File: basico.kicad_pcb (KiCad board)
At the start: 2 copper layers, 85.7 x 60.3 mm, 14 parts, among them P1 Power, P10 CONN_01X01, P11 CONN_01X01, P12 CONN_01X01, P13 CONN_01X01, P2 Analog, P3 Analog, P4 Digital, P5 PWM, P6 PWM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

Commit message: Update PCB
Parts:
- moved P4 91.6 mm to (82.0, 126.5)
- moved P3 59.1 mm to (81.0, 101.0), turned to 270 degrees
- moved P7 56.4 mm to (126.0, 103.0), turned to 270 degrees
- moved P6 50.9 mm to (124.5, 78.5), turned to 270 degrees
- moved P5 44.3 mm to (125.0, 50.5), turned to 270 degrees
- moved P2 31.0 mm to (81.0, 77.5), turned to 270 degrees
- moved P1 29.3 mm to (81.0, 50.5), turned to 270 degrees
- moved P10 21.4 mm to (101.1, 36.2)
- moved P11 21.4 mm to (106.8, 36.2)
- moved P12 21.4 mm to (112.5, 36.2)
- moved P13 21.4 mm to (118.2, 36.2)
- moved P8 21.4 mm to (89.6, 36.2)
- moved P9 21.4 mm to (95.4, 36.2)
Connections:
- P2 pad 1: (no net) -> /Ar_A0
- P2 pad 2: (no net) -> /Ar_A1
- P2 pad 3: (no net) -> /Ar_A2
- P2 pad 4: (no net) -> /Ar_A3
- P2 pad 5: (no net) -> /Ar_A4
- P2 pad 6: (no net) -> /Ar_A5
- P2 pad 7: (no net) -> /Ar_A6
- P2 pad 8: (no net) -> /Ar_A7
- P3 pad 1: (no net) -> /Ar_A8
- P3 pad 6: (no net) -> /Ar_A13
- P4 pad 11: (no net) -> /Ar_44
- P4 pad 13: (no net) -> /Ar_42
- P4 pad 15: (no net) -> /Ar_40
- P4 pad 17: (no net) -> /Ar_38
- P4 pad 19: (no net) -> /Ar_36
- P4 pad 21: (no net) -> /Ar_34
- P4 pad 25: (no net) -> /Ar_30
- P4 pad 27: (no net) -> /Ar_28
- P4 pad 29: (no net) -> /Ar_26
- P4 pad 3: (no net) -> /Ar_52
- P4 pad 31: (no net) -> /Ar_24
- P4 pad 4: (no net) -> /Ar_53
- P4 pad 5: (no net) -> /Ar_50
- P4 pad 6: (no net) -> /Ar_51
- P4 pad 7: (no net) -> /Ar_48
- P4 pad 8: (no net) -> /Ar_49
- P4 pad 9: (no net) -> /Ar_46
- P5 pad 10: (no net) -> /Ar_8
- P5 pad 7: (no net) -> /Ar_11
- P5 pad 8: (no net) -> /Ar_10
- P5 pad 9: (no net) -> /Ar_9
- P6 pad 4: (no net) -> /Ar_4
- P6 pad 5: (no net) -> /Ar_3
- P7 pad 1: (no net) -> /Ar_14
- P7 pad 3: (no net) -> /Ar_16
- P7 pad 4: (no net) -> /Ar_17
- P7 pad 5: (no net) -> /Ar_18
- P7 pad 7: (no net) -> /Ar_20
- P7 pad 8: (no net) -> /Ar_21
- XA101 pad 11: (no net) -> /Ar_10
- XA101 pad 13: (no net) -> /Ar_9
- XA101 pad 19: (no net) -> /Ar_20
- XA101 pad 21: (no net) -> /Ar_21
- XA101 pad 23: (no net) -> /Ar_8
- XA101 pad 25: (no net) -> /Ar_9
- XA101 pad 27: (no net) -> /Ar_10
- XA101 pad 29: (no net) -> /Ar_30
- XA101 pad 31: (no net) -> /Ar_3
- XA101 pad 33: (no net) -> /Ar_18
- XA101 pad 34: (no net) -> /Ar_34
- XA101 pad 35: (no net) -> /Ar_24
- XA101 pad 36: (no net) -> /Ar_26
- XA101 pad 37: (no net) -> /Ar_28
- XA101 pad 39: (no net) -> /Ar_14
- XA101 pad 44: (no net) -> /Ar_A0
- XA101 pad 46: (no net) -> /Ar_A1
- XA101 pad 48: (no net) -> /Ar_A2
- XA101 pad 49: (no net) -> /Ar_A6
- XA101 pad 50: (no net) -> /Ar_A7
- XA101 pad 52: (no net) -> /Ar_A8
- XA101 pad 54: (no net) -> /Ar_11
- XA101 pad 56: (no net) -> /Ar_4
- XA101 pad 58: (no net) -> /Ar_50
- XA101 pad 60: (no net) -> /Ar_52
- XA101 pad 61: (no net) -> /Ar_51
- XA101 pad 62: (no net) -> /Ar_A13
- XA101 pad 63: (no net) -> /Ar_17
- XA101 pad 64: (no net) -> /Ar_16
- XA101 pad 66: (no net) -> /Ar_A3
- XA101 pad 68: (no net) -> /Ar_44
- XA101 pad 69: (no net) -> /Ar_38
- XA101 pad 70: (no net) -> /Ar_A5
- XA101 pad 71: (no net) -> /Ar_48
- XA101 pad 72: (no net) -> /Ar_46
- XA101 pad 73: (no net) -> /Ar_A4
- XA101 pad 74: (no net) -> /Ar_36
- XA101 pad 75: (no net) -> /Ar_42
- XA101 pad 76: (no net) -> /Ar_40
- XA101 pad 78: (no net) -> /Ar_49
- XA101 pad 80: (no net) -> /Ar_53
- XA101 pad 9: (no net) -> /Ar_11

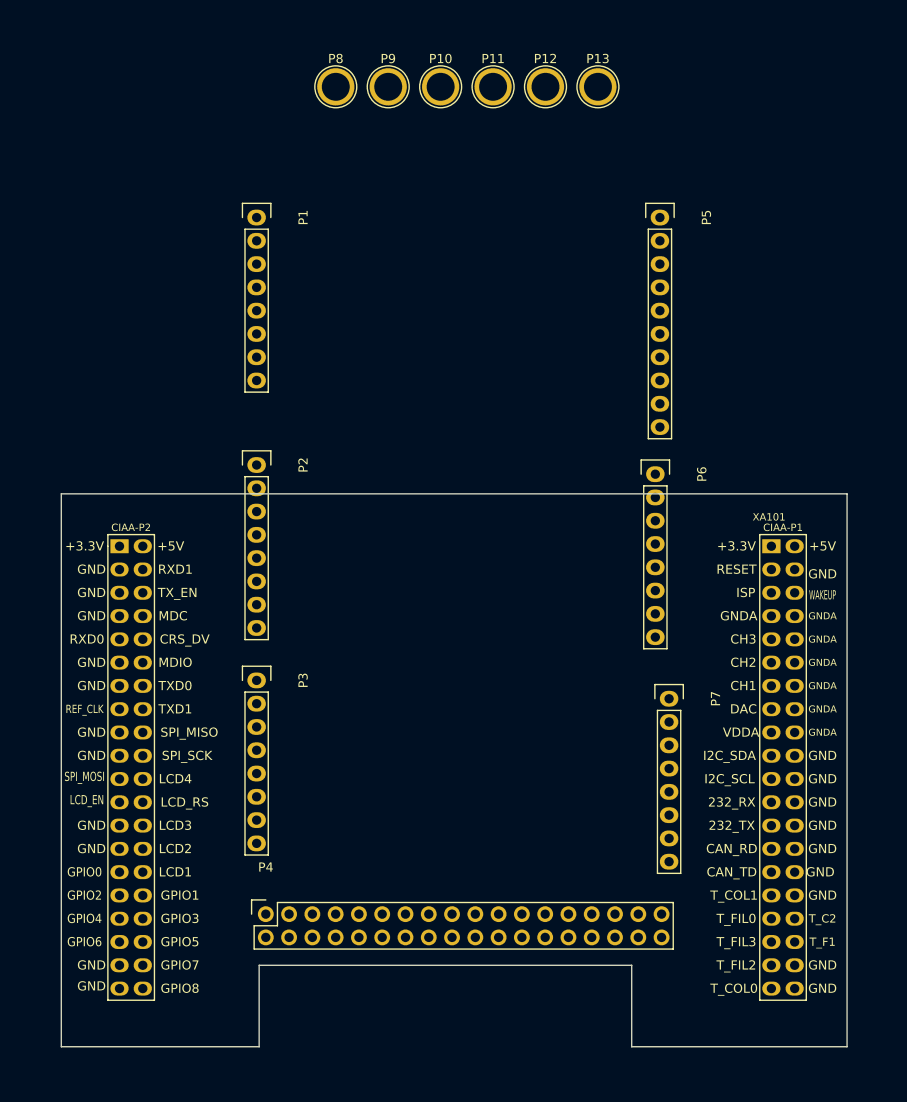
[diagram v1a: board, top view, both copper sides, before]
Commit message: Remove unused components. Update PCB
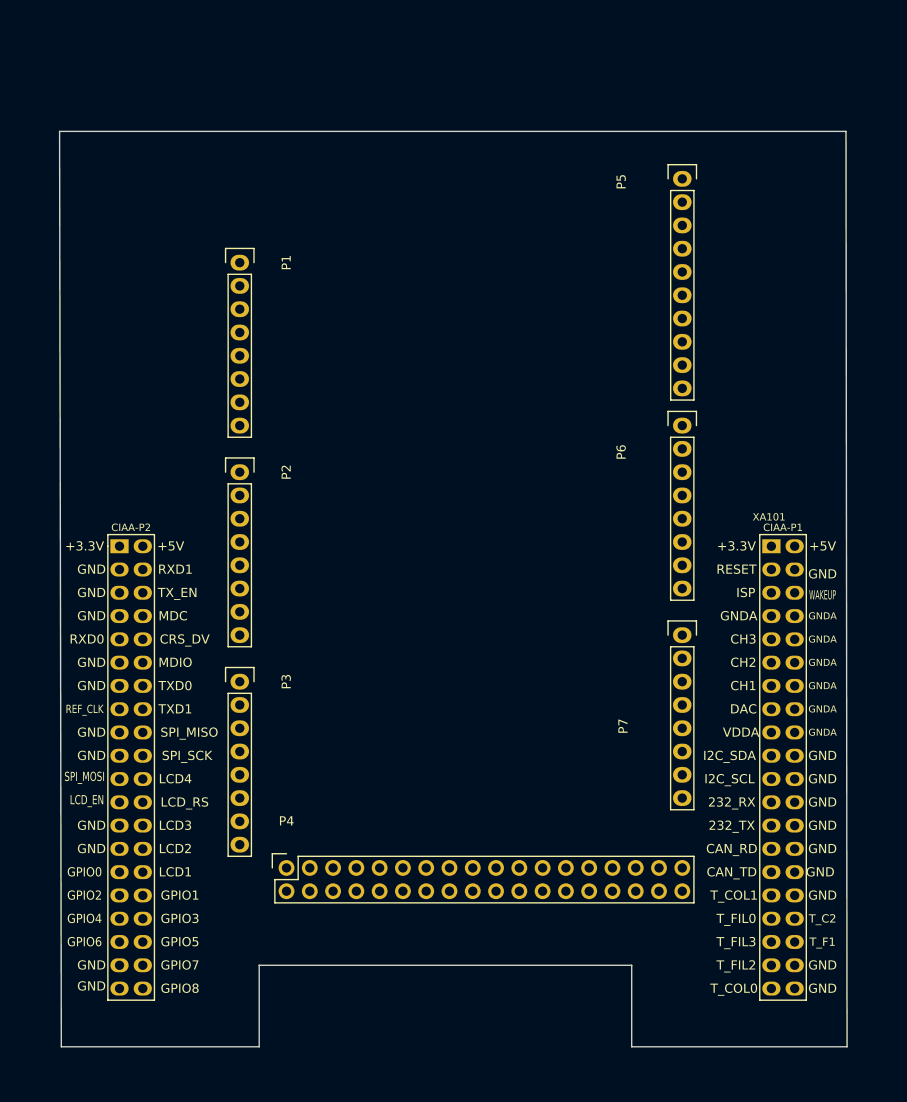
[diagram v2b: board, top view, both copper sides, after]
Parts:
- removed P10, P11, P12, P13, P8, P9: CONN_01X01, footprint:Arduino_1pin
- moved P7 7.09 mm to (127.4, 96.1)
- moved P6 6.06 mm to (127.4, 73.2)
- moved P4 5.52 mm to (84.3, 121.5)
- moved P1 5.25 mm to (79.2, 55.4)
- moved P5 4.87 mm to (127.4, 46.3)
- moved P2 2.00 mm to (79.2, 78.3)
- moved P3 1.85 mm to (79.2, 101.1)
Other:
- board size 85.7 x 60.3 mm -> 85.9 x 99.9 mm
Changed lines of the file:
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@@
     (tracks 0)
     (zones 0)
-    (modules 14)
+    (modules 8)
     (nets 44)
   )
@@
     (add_net +3.3VP)
     (add_net +5V)
-    (add_net /Ar_0)
-    (add_net /Ar_1)
     (add_net /Ar_10)
     (add_net /Ar_11)
-    (add_net /Ar_12)
-    (add_net /Ar_13)
     (add_net /Ar_14)
-    (add_net /Ar_15)
     (add_net /Ar_16)
     (add_net /Ar_17)
     (add_net /Ar_18)
-    (add_net /Ar_19)
-    (add_net /Ar_2)
     (add_net /Ar_20)
     (add_net /Ar_21)
-    (add_net /Ar_22)
-    (add_net /Ar_23)
     (add_net /Ar_24)
-    (add_net /Ar_25)
     (add_net /Ar_26)
-    (add_net /Ar_27)
     (add_net /Ar_28)
-    (add_net /Ar_29)
     (add_net /Ar_3)
     (add_net /Ar_30)
-    (add_net /Ar_31)
-    (add_net /Ar_32)
-    (add_net /Ar_33)
     (add_net /Ar_34)
-    (add_net /Ar_35)
     (add_net /Ar_36)
-    (add_net /Ar_37)
     (add_net /Ar_38)
-    (add_net /Ar_39)
     (add_net /Ar_4)
     (add_net /Ar_40)
-    (add_net /Ar_41)
     (add_net /Ar_42)
-    (add_net /Ar_43)
     (add_net /Ar_44)
-    (add_net /Ar_45)
     (add_net /Ar_46)
-    (add_net /Ar_47)
     (add_net /Ar_48)
     (add_net /Ar_49)
-    (add_net /Ar_5)
     (add_net /Ar_50)
     (add_net /Ar_51)
     (add_net /Ar_52)
     (add_net /Ar_53)
-    (add_net /Ar_6)
-    (add_net /Ar_7)
     (add_net /Ar_8)
     (add_net /Ar_9)
     (add_net /Ar_A0)
     (add_net /Ar_A1)
-    (add_net /Ar_A10)
-    (add_net /Ar_A11)
-    (add_net /Ar_A12)
     (add_net /Ar_A13)
-    (add_net /Ar_A14)
-    (add_net /Ar_A15)
     (add_net /Ar_A2)
     (add_net /Ar_A3)
@@
     (add_net /Ar_A7)
     (add_net /Ar_A8)
-    (add_net /Ar_A9)
-    (add_net /Ar_AREF)
-    (add_net /Ar_IOREF)
-    (add_net /Ar_Reset)
-    (add_net /Ar_SCL)
-    (add_net /Ar_SDA)
-    (add_net /Ar_Vin)
     (add_net GND)
     (add_net GNDA)
-    (add_net "Net-(P1-Pad1)")
-    (add_net "Net-(P10-Pad1)")
-    (add_net "Net-(P11-Pad1)")
-    (add_net "Net-(P12-Pad1)")
-    (add_net "Net-(P13-Pad1)")
-    (add_net "Net-(P8-Pad1)")
-    (add_net "Net-(P9-Pad1)")
-    (add_net "Net-(XA101-Pad15)")
-    (add_net "Net-(XA101-Pad17)")
-    (add_net "Net-(XA101-Pad3)")
-    (add_net "Net-(XA101-Pad5)")
-    (add_net "Net-(XA101-Pad55)")
-    (add_net "Net-(XA101-Pad6)")
-  )
-  (module footprint:Arduino_1pin (layer F.Cu)
-    (at 118.236 36.236)
-    (descr "module 1 pin (ou trou mecanique de percage)")
-    (tags DEV)
-    (fp_text reference P13 (at 0 -3.048) (layer F.SilkS)
-      (effects (font (size 1 1) (thickness 0.15)))
-    )
-    (fp_text value CONN_01X01 (at 0 2.794) (layer F.Fab)
-      (effects (font (size 1 1) (thickness 0.15)))
-    )
-    (fp_circle (center 0 0) (end 0 -2.286) (layer F.SilkS) (width 0.15))
-    (pad 1 thru_hole circle (at 0 0) (size 4.064 4.064) (drill 3.048) (layers *.Cu *.Mask F.SilkS))
-  )
-  (module footprint:Arduino_1pin (layer F.Cu)
-    (at 112.516 36.236)
-    (descr "module 1 pin (ou trou mecanique de percage)")
-    (tags DEV)
-    (fp_text reference P12 (at 0 -3.048) (layer F.SilkS)
-      (effects (font (size 1 1) (thickness 0.15)))
-    )
-    (fp_text value CONN_01X01 (at 0 2.794) (layer F.Fab)
-      (effects (font (size 1 1) (thickness 0.15)))
-    )
-    (fp_circle (center 0 0) (end 0 -2.286) (layer F.SilkS) (width 0.15))
-    (pad 1 thru_hole circle (at 0 0) (size 4.064 4.064) (drill 3.048) (layers *.Cu *.Mask F.SilkS))
-  )
-  (module footprint:Arduino_1pin (layer F.Cu)
-    (at 106.796 36.236)
-    (descr "module 1 pin (ou trou mecanique de percage)")
-    (tags DEV)
-    (fp_text reference P11 (at 0 -3.048) (layer F.SilkS)
-      (effects (font (size 1 1) (thickness 0.15)))
-    )
-    (fp_text value CONN_01X01 (at 0 2.794) (layer F.Fab)
-      (effects (font (size 1 1) (thickness 0.15)))
-    )
-    (fp_circle (center 0 0) (end 0 -2.286) (layer F.SilkS) (width 0.15))
-    (pad 1 thru_hole circle (at 0 0) (size 4.064 4.064) (drill 3.048) (layers *.Cu *.Mask F.SilkS))
-  )
-  (module footprint:Arduino_1pin (layer F.Cu)
-    (at 101.076 36.236)
-    (descr "module 1 pin (ou trou mecanique de percage)")
-    (tags DEV)
-    (fp_text reference P10 (at 0 -3.048) (layer F.SilkS)
-      (effects (font (size 1 1) (thickness 0.15)))
-    )
-    (fp_text value CONN_01X01 (at 0 2.794) (layer F.Fab)
-      (effects (font (size 1 1) (thickness 0.15)))
-    )
-    (fp_circle (center 0 0) (end 0 -2.286) (layer F.SilkS) (width 0.15))
-    (pad 1 thru_hole circle (at 0 0) (size 4.064 4.064) (drill 3.048) (layers *.Cu *.Mask F.SilkS))
-  )
-  (module footprint:Arduino_1pin (layer F.Cu)
-    (at 95.356 36.236)
-    (descr "module 1 pin (ou trou mecanique de percage)")
-    (tags DEV)
-    (fp_text reference P9 (at 0 -3.048) (layer F.SilkS)
-      (effects (font (size 1 1) (thickness 0.15)))
-    )
-    (fp_text value CONN_01X01 (at 0 2.794) (layer F.Fab)
-      (effects (font (size 1 1) (thickness 0.15)))
-    )
-    (fp_circle (center 0 0) (end 0 -2.286) (layer F.SilkS) (width 0.15))
-    (pad 1 thru_hole circle (at 0 0) (size 4.064 4.064) (drill 3.048) (layers *.Cu *.Mask F.SilkS))
-  )
-  (module footprint:Arduino_1pin (layer F.Cu)
-    (at 89.636 36.236)
-    (descr "module 1 pin (ou trou mecanique de percage)")
-    (tags DEV)
-    (fp_text reference P8 (at 0 -3.048) (layer F.SilkS)
-      (effects (font (size 1 1) (thickness 0.15)))
-    )
-    (fp_text value CONN_01X01 (at 0 2.794) (layer F.Fab)
-      (effects (font (size 1 1) (thickness 0.15)))
-    )
-    (fp_circle (center 0 0) (end 0 -2.286) (layer F.SilkS) (width 0.15))
-    (pad 1 thru_hole circle (at 0 0) (size 4.064 4.064) (drill 3.048) (layers *.Cu *.Mask F.SilkS))
   )
   (module footprint:Socket_Strip_Arduino_1x08 (layer F.Cu)
-    (at 126 103 270)
+    (at 127.435 96.06 270)
     (descr "Through hole socket strip")
     (tags "socket strip")
-    (fp_text reference P7 (at 0 -5.1 90) (layer F.SilkS)
-      (effects (font (size 1 1) (thickness 0.15)))
-    )
-    (fp_text value Communication (at 0 -3.1 90) (layer F.Fab)
+    (fp_text reference P7 (at 9.94 6.435 90) (layer F.SilkS)
+      (effects (font (size 1 1) (thickness 0.15)))
+    )
+    (fp_text value Communication (at 9.04 4.435 90) (layer F.Fab)
       (effects (font (size 1 1) (thickness 0.15)))
     )
@@
   )
   (module footprint:Socket_Strip_Arduino_1x08 (layer F.Cu)
-    (at 124.5 78.5 270)
+    (at 127.435 73.2 270)
     (descr "Through hole socket strip")
     (tags "socket strip")
-    (fp_text reference P6 (at 0 -5.1 90) (layer F.SilkS)
-      (effects (font (size 1 1) (thickness 0.15)))
-    )
-    (fp_text value PWM (at 0 -3.1 90) (layer F.Fab)
+    (fp_text reference P6 (at 2.9 6.635 90) (layer F.SilkS)
+      (effects (font (size 1 1) (thickness 0.15)))
+    )
+    (fp_text value PWM (at 2.4 4.335 90) (layer F.Fab)
       (effects (font (size 1 1) (thickness 0.15)))
     )
@@
   )
   (module footprint:Socket_Strip_Arduino_1x10 (layer F.Cu)
-    (at 125 50.5 270)
+    (at 127.44 46.28 270)
     (descr "Through hole socket strip")
     (tags "socket strip")
-    (fp_text reference P5 (at 0 -5.1 90) (layer F.SilkS)
-      (effects (font (size 1 1) (thickness 0.15)))
-    )
-    (fp_text value PWM (at 0 -3.1 90) (layer F.Fab)
+    (fp_text reference P5 (at 0.32 6.64 90) (layer F.SilkS)
+      (effects (font (size 1 1) (thickness 0.15)))
+    )
+    (fp_text value PWM (at 0.42 4.34 90) (layer F.Fab)
       (effects (font (size 1 1) (thickness 0.15)))
     )
@@
   )
   (module footprint:Socket_Strip_Arduino_2x18 (layer F.Cu)
-    (at 82 126.5)
+    (at 84.26 121.46)
     (descr "Through hole socket strip")
     (tags "socket strip")
@@
   )
   (module footprint:Socket_Strip_Arduino_1x08 (layer F.Cu)
-    (at 81 101 270)
+    (at 79.16 101.14 270)
     (descr "Through hole socket strip")
     (tags "socket strip")
@@
   )
   (module footprint:Socket_Strip_Arduino_1x08 (layer F.Cu)
-    (at 81 77.5 270)
+    (at 79.16 78.28 270)
     (descr "Through hole socket strip")
     (tags "socket strip")
@@
   )
   (module footprint:Socket_Strip_Arduino_1x08 (layer F.Cu)
-    (at 81 50.5 270)
+    (at 79.16 55.42 270)
     (descr "Through hole socket strip")
     (tags "socket strip")
@@
     )
   )
-  (gr_line (start 59.69 140.97) (end 59.69 80.645) (angle 90) (layer Edge.Cuts) (width 0.15))
+  (gr_line (start 59.69 140.97) (end 59.5 41.1) (angle 90) (layer Edge.Cuts) (width 0.15))
   (gr_line (start 81.28 140.97) (end 59.69 140.97) (angle 90) (layer Edge.Cuts) (width 0.15))
   (gr_line (start 81.28 132.08) (end 81.28 140.97) (angle 90) (layer Edge.Cuts) (width 0.15))
@@
   (gr_line (start 121.92 140.97) (end 121.92 132.08) (angle 90) (layer Edge.Cuts) (width 0.15))
   (gr_line (start 145.415 140.97) (end 121.92 140.97) (angle 90) (layer Edge.Cuts) (width 0.15))
-  (gr_line (start 145.415 80.645) (end 145.415 140.97) (angle 90) (layer Edge.Cuts) (width 0.15))
-  (gr_line (start 59.69 80.645) (end 145.415 80.645) (angle 90) (layer Edge.Cuts) (width 0.15))
+  (gr_line (start 145.3 41.1) (end 145.415 140.97) (angle 90) (layer Edge.Cuts) (width 0.15))
+  (gr_line (start 59.5 41.1) (end 145.3 41.1) (angle 90) (layer Edge.Cuts) (width 0.15))
   (gr_line (start 228.6 163.83) (end 227.965 163.195) (angle 90) (layer Dwgs.User) (width 0.2))
   (gr_line (start 229.235 163.195) (end 228.6 163.83) (angle 90) (layer Dwgs.User) (width 0.2))

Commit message: Fix wrong mapping for analog channels
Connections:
- P3 pad 2: (no net) -> /Ar_A9
- P3 pad 3: (no net) -> /Ar_A10
- P3 pad 4: (no net) -> /Ar_A11
- XA101 pad 11: /Ar_10 -> /Ar_A10
- XA101 pad 13: /Ar_9 -> /Ar_A9
- XA101 pad 9: /Ar_11 -> /Ar_A11
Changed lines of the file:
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@@
     (zones 0)
     (modules 8)
-    (nets 44)
+    (nets 47)
   )
   (page A4)
@@
   (net 42 /Ar_16)
   (net 43 /Ar_14)
+  (net 44 /Ar_A11)
+  (net 45 /Ar_A10)
+  (net 46 /Ar_A9)
   (net_class Default "This is the default net class."
     (clearance 0.51)
@@
     (add_net +3.3VP)
     (add_net +5V)
+    (add_net /Ar_0)
+    (add_net /Ar_1)
     (add_net /Ar_10)
     (add_net /Ar_11)
+    (add_net /Ar_12)
+    (add_net /Ar_13)
     (add_net /Ar_14)
+    (add_net /Ar_15)
     (add_net /Ar_16)
     (add_net /Ar_17)
     (add_net /Ar_18)
+    (add_net /Ar_19)
+    (add_net /Ar_2)
     (add_net /Ar_20)
     (add_net /Ar_21)
+    (add_net /Ar_22)
+    (add_net /Ar_23)
     (add_net /Ar_24)
+    (add_net /Ar_25)
     (add_net /Ar_26)
+    (add_net /Ar_27)
     (add_net /Ar_28)
+    (add_net /Ar_29)
     (add_net /Ar_3)
     (add_net /Ar_30)
+    (add_net /Ar_31)
+    (add_net /Ar_32)
+    (add_net /Ar_33)
     (add_net /Ar_34)
+    (add_net /Ar_35)
     (add_net /Ar_36)
+    (add_net /Ar_37)
     (add_net /Ar_38)
+    (add_net /Ar_39)
     (add_net /Ar_4)
     (add_net /Ar_40)
+    (add_net /Ar_41)
     (add_net /Ar_42)
+    (add_net /Ar_43)
     (add_net /Ar_44)
+    (add_net /Ar_45)
     (add_net /Ar_46)
+    (add_net /Ar_47)
     (add_net /Ar_48)
     (add_net /Ar_49)
+    (add_net /Ar_5)
     (add_net /Ar_50)
     (add_net /Ar_51)
     (add_net /Ar_52)
     (add_net /Ar_53)
+    (add_net /Ar_6)
+    (add_net /Ar_7)
     (add_net /Ar_8)
     (add_net /Ar_9)
     (add_net /Ar_A0)
     (add_net /Ar_A1)
+    (add_net /Ar_A10)
+    (add_net /Ar_A11)
+    (add_net /Ar_A12)
     (add_net /Ar_A13)
+    (add_net /Ar_A14)
+    (add_net /Ar_A15)
     (add_net /Ar_A2)
     (add_net /Ar_A3)
@@
     (add_net /Ar_A7)
     (add_net /Ar_A8)
+    (add_net /Ar_A9)
+    (add_net /Ar_AREF)
+    (add_net /Ar_IOREF)
+    (add_net /Ar_Reset)
+    (add_net /Ar_SCL)
+    (add_net /Ar_SDA)
+    (add_net /Ar_Vin)
     (add_net GND)
     (add_net GNDA)
+    (add_net "Net-(P1-Pad1)")
+    (add_net "Net-(XA101-Pad15)")
+    (add_net "Net-(XA101-Pad17)")
+    (add_net "Net-(XA101-Pad3)")
+    (add_net "Net-(XA101-Pad5)")
+    (add_net "Net-(XA101-Pad55)")
+    (add_net "Net-(XA101-Pad6)")
   )
   (module footprint:Socket_Strip_Arduino_1x08 (layer F.Cu)
@@
       (net 13 /Ar_A13))
     (pad 5 thru_hole oval (at 10.16 0 270) (size 1.7272 2.032) (drill 1.016) (layers *.Cu *.Mask F.SilkS))
-    (pad 4 thru_hole oval (at 7.62 0 270) (size 1.7272 2.032) (drill 1.016) (layers *.Cu *.Mask F.SilkS))
-    (pad 3 thru_hole oval (at 5.08 0 270) (size 1.7272 2.032) (drill 1.016) (layers *.Cu *.Mask F.SilkS))
-    (pad 2 thru_hole oval (at 2.54 0 270) (size 1.7272 2.032) (drill 1.016) (layers *.Cu *.Mask F.SilkS))
+    (pad 4 thru_hole oval (at 7.62 0 270) (size 1.7272 2.032) (drill 1.016) (layers *.Cu *.Mask F.SilkS)
+      (net 44 /Ar_A11))
+    (pad 3 thru_hole oval (at 5.08 0 270) (size 1.7272 2.032) (drill 1.016) (layers *.Cu *.Mask F.SilkS)
+      (net 45 /Ar_A10))
+    (pad 2 thru_hole oval (at 2.54 0 270) (size 1.7272 2.032) (drill 1.016) (layers *.Cu *.Mask F.SilkS)
+      (net 46 /Ar_A9))
     (pad 1 thru_hole oval (at 0 0 270) (size 1.7272 2.032) (drill 1.016) (layers *.Cu *.Mask F.SilkS)
       (net 14 /Ar_A8))
@@
       (net 1 +5V))
     (pad 11 thru_hole oval (at 0 12.7 270) (size 1.524 2) (drill 1.016) (layers *.Cu *.Mask F.SilkS)
-      (net 34 /Ar_10))
+      (net 45 /Ar_A10))
     (pad 4 thru_hole oval (at 2.54 2.54 270) (size 1.524 2) (drill 1.016) (layers *.Cu *.Mask F.SilkS)
       (net 2 GND))
     (pad 13 thru_hole oval (at 0 15.24 270) (size 1.524 2) (drill 1.016) (layers *.Cu *.Mask F.SilkS)
-      (net 33 /Ar_9))
+      (net 46 /Ar_A9))
     (pad 6 thru_hole oval (at 2.54 5.08 270) (size 1.524 2) (drill 1.016) (layers *.Cu *.Mask F.SilkS))
     (pad 15 thru_hole oval (at 0 17.78 270) (size 1.524 2) (drill 1.016) (layers *.Cu *.Mask F.SilkS))
@@
       (net 4 GNDA))
     (pad 9 thru_hole oval (at 0 10.16 270) (size 1.524 2) (drill 1.016) (layers *.Cu *.Mask F.SilkS)
-      (net 35 /Ar_11))
+      (net 44 /Ar_A11))
     (pad 39 thru_hole oval (at 0 48.26 270) (size 1.524 2) (drill 1.016) (layers *.Cu *.Mask F.SilkS)
       (net 43 /Ar_14))
